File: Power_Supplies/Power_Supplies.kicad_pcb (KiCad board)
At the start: 4 copper layers, 322 parts, among them IC1 PCM1865DBT, IC2 LT8338, IC5 PCM1865DBT, J1 Line Out (Left), J10 XLR3_AudioJack3_Combo, J2 Headphone Out, J20 ACJM-MV-2, J21 Line Out (Right), J22 2171790001, J3 XLR3_AudioJack3_Combo, J4 XLR3_AudioJack3_Combo, J5 ACJM-MV-2, J6 ACJM-MV-2, J7 ACJM-MV-2, J8 FTSH-110-01-F-DV-K, J9 XLR3_AudioJack3_Combo, SW1 SW_Push, SW2 SW_Push, SW3 SW_Push, SW4 SW_Push, U1 TPS62822DLC, U10 OPA2134, U11 TPA6110A2DGN, U12 XU316-1024-TQ128-I24, U13 Si5351A-B-GT, U14 W25Q64JVSSIQ (FLASH MEMORY), U15 OPA2134, U16 SSM2019BRNZ, U17 SSM2019BRNZ, U18 OPA2134, U19 SSM2019BRNZ, U2 TPS73601DBV, U20 SSM2019BRNZ, U3 TPS62822DLC, U34 NE5532AD, U35 NE5532AD, U37 PEC11R-4030F-N0024, U4 TPS73601DBV, U5 NCP1117-5.0_SOT223, U6 TPS82140, U7 TPS62822DLC, U8 LM27761, U9 PCM1780, X1 FA-238 24.0000MB-C0 (CRYSTAL), X2 FA-238 24.0000MB-C0

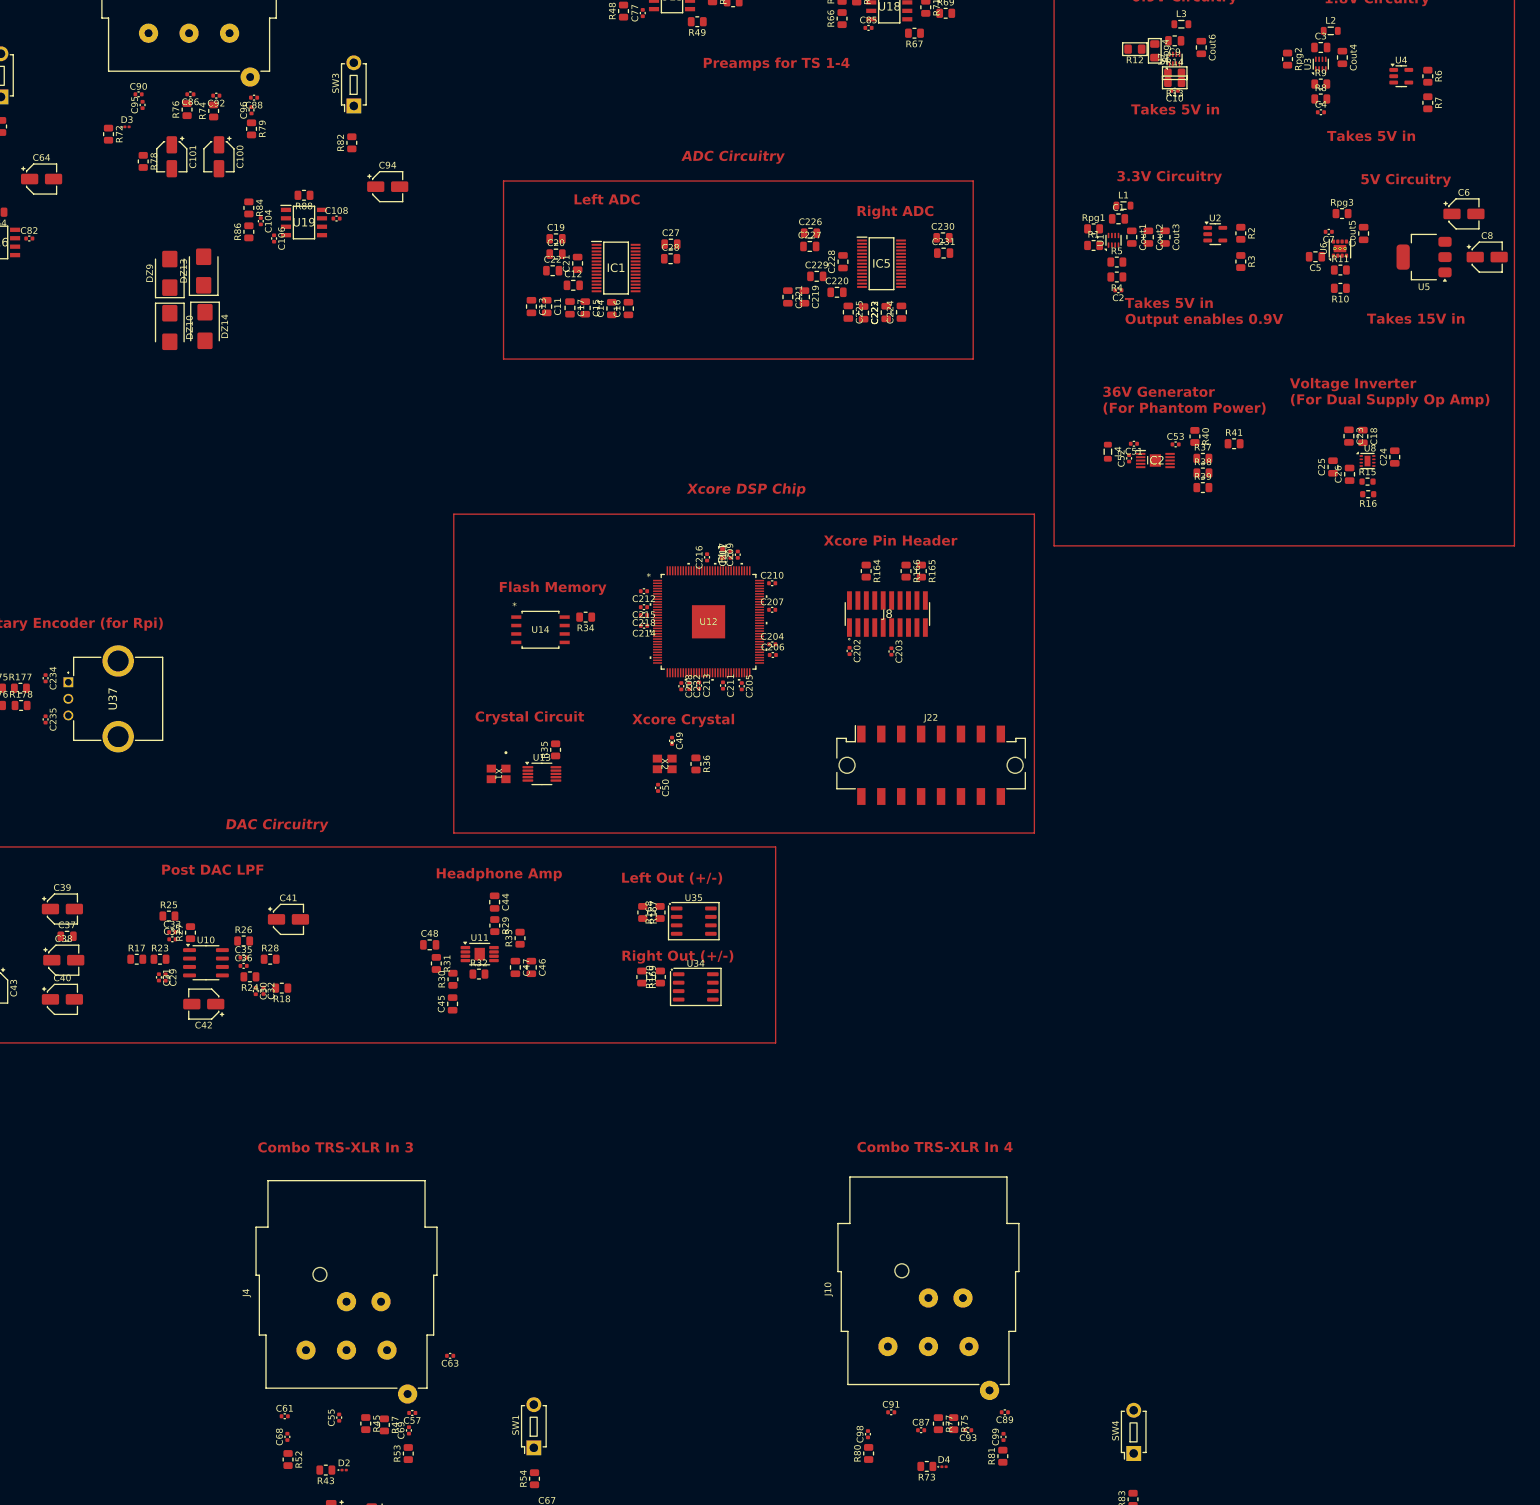
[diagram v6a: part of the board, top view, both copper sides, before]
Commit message: Added stuff for the power supply circuitry
changed all grounds to GND (same ground plane)
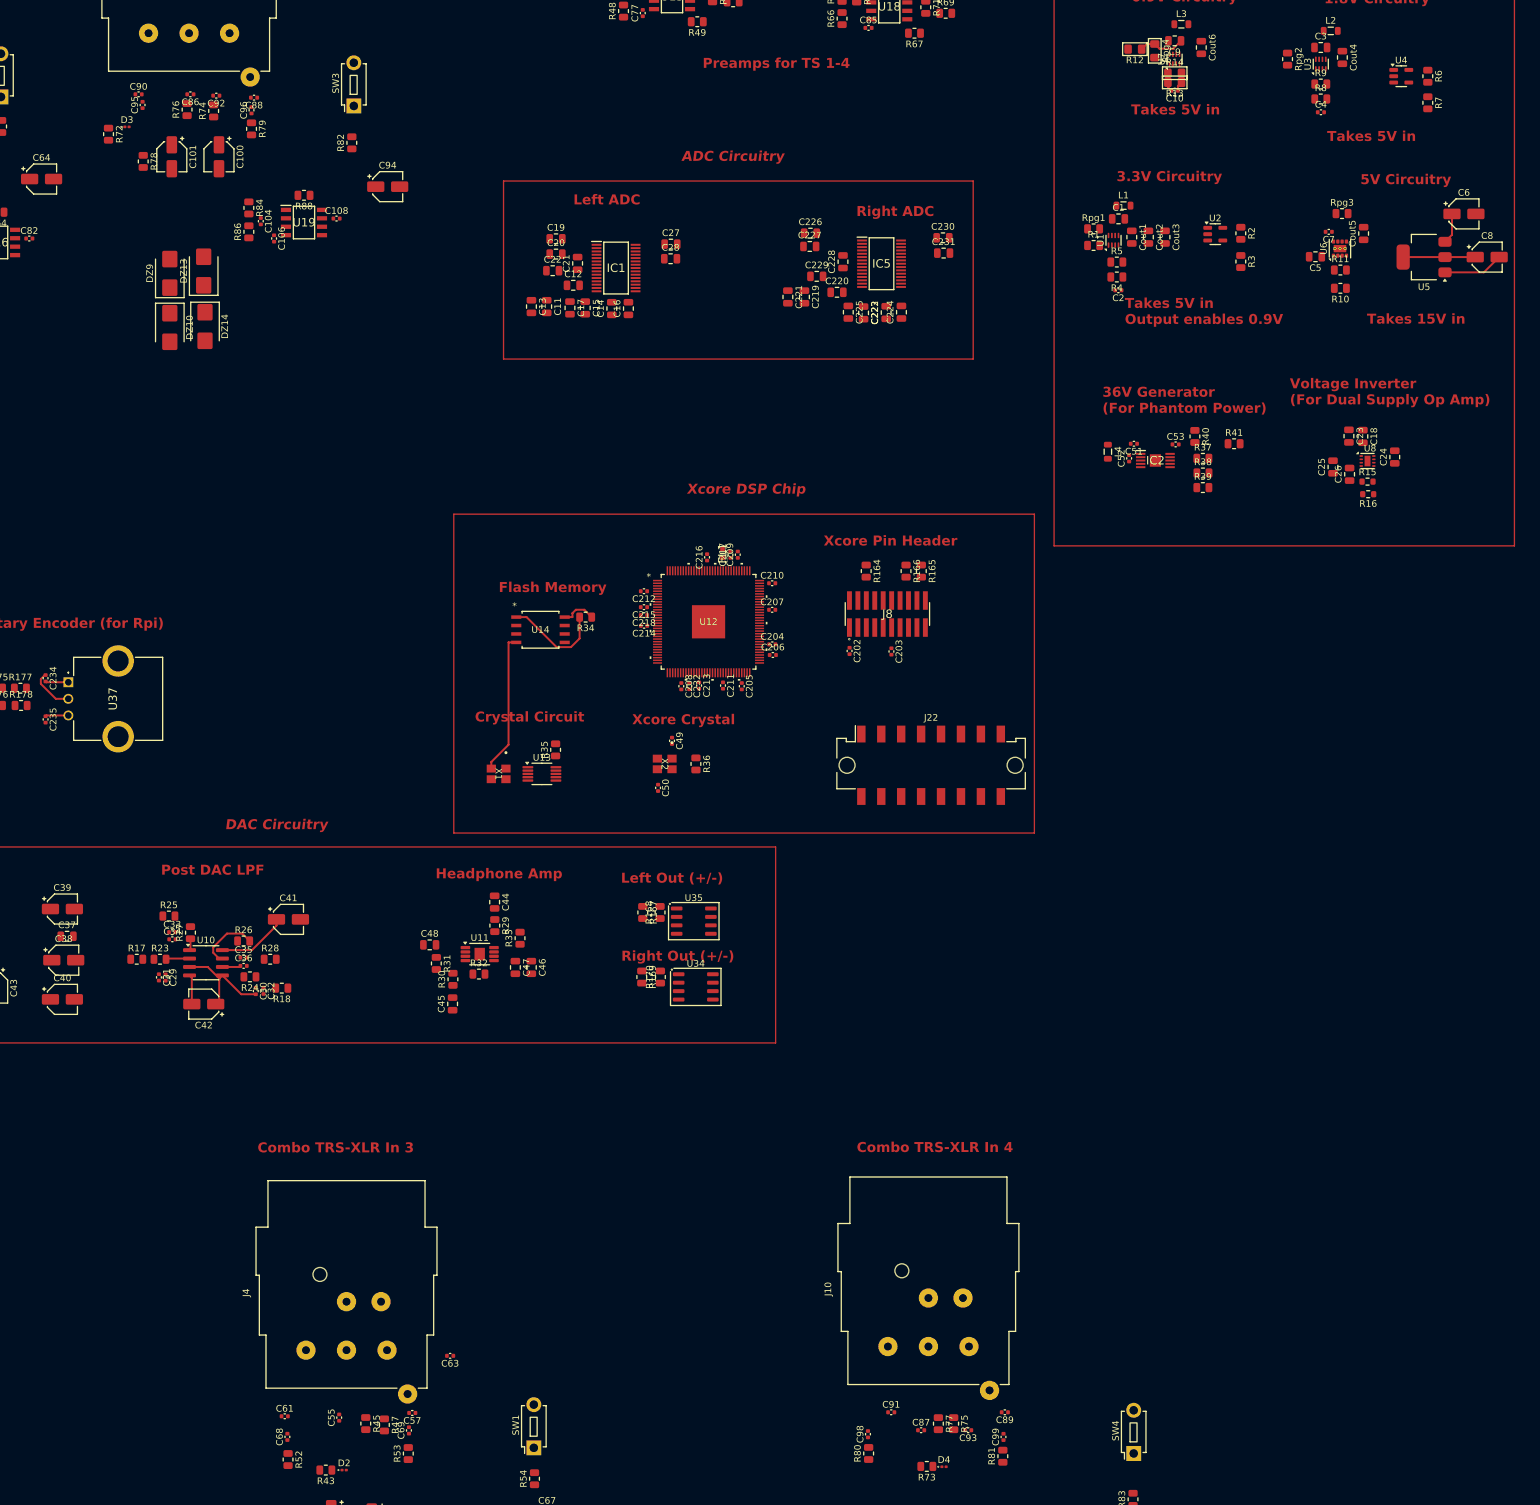
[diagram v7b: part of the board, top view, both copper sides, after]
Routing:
- net AGND: track 0.00 -> 54.7 mm
- net 5V: track 0.00 -> 17.6 mm
- net QSPI_CS_N: track 0.00 -> 15.2 mm
- net 5V_LDO: track 0.00 -> 10.8 mm
- net Net-(C35-Pad2): track 0.00 -> 9.36 mm
- net 3.3V: track 0.00 -> 5.33 mm
- net 15V: track 0.00 -> 4.63 mm
- net -5V: track 0.00 -> 4.46 mm
- net Net-(U10A--): track 0.00 -> 3.57 mm
- net Net-(U37-CHANNEL_2): track 0.00 -> 3.47 mm
- net Net-(U37-CHANNEL_1): track 0.00 -> 3.47 mm
- net /0.9V Power Supply/V_FB: track 0.00 -> 2.86 mm
- net Net-(U10B--): track 0.00 -> 2.78 mm
- net Net-(C33-Pad2): track 0.00 -> 1.77 mm
- net 0.9V: track 0.00 -> 1.48 mm

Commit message: Add files via upload
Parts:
- removed C1, C25, C3, C9: 4.7uF, Capacitor_SMD:C_0805_2012Metric
- removed C10, C2, C4: 120pF, Capacitor_SMD:C_0402_1005Metric
- removed C18: 10uF, Capacitor_SMD:C_0805_2012Metric
- removed C23, C24: 1uF, Capacitor_SMD:C_0805_2012Metric
- removed C26: 2.2uF, Capacitor_SMD:C_0805_2012Metric
- removed C5, Cout1, Cout2, Cout3, Cout4, Cout6: 22uF, Capacitor_SMD:C_0805_2012Metric
- removed C51, C52, C53: 2.2uF, Capacitor_SMD:C_0402_1005Metric
- removed C6, C8: 10uF, Capacitor_SMD:CP_Elec_4x5.8
- removed C7: 430pF, Capacitor_SMD:C_0402_1005Metric
- removed Cout5: 47uF, Capacitor_SMD:C_0805_2012Metric
- removed D1, D2, D3, D4: LED, LED_SMD:LED_0201_0603Metric
- removed IC2: LT8338, SamacSys_Parts:SOP50P490X110-11N
- removed L1, L2, L3: 470nH, Inductor_SMD:L_0805_2012Metric
- removed L4: 10uH, Inductor_SMD:L_0805_2012Metric
- removed R1: 20k, Resistor_SMD:R_0805_2012Metric
- removed R10: 523k, Resistor_SMD:R_0805_2012Metric
- removed R11, R5, R9, Rpg1, Rpg2, Rpg3: 100k, Resistor_SMD:R_0805_2012Metric
- removed R12: 10k, PCM_Resistor_SMD_AKL:R_0805_2012Metric_Pad1.15x1.40mm_HandSolder
- removed R13: 49.9k, PCM_Resistor_SMD_AKL:R_0805_2012Metric_Pad1.15x1.40mm_HandSolder
- removed R14, Rpg4: 100k, PCM_Resistor_SMD_AKL:R_0805_2012Metric_Pad1.15x1.40mm_HandSolder
- removed R15: 249k, Resistor_SMD:R_0603_1608Metric
- removed R16: 499k, Resistor_SMD:R_0603_1608Metric
- removed R2: 52.3k, Resistor_SMD:R_0805_2012Metric
- removed R3: 30.1k, Resistor_SMD:R_0805_2012Metric
- removed R37, R41: 1M, Resistor_SMD:R_0805_2012Metric
- removed R38: 162k, Resistor_SMD:R_0805_2012Metric
- removed R39: 40.2k, Resistor_SMD:R_0805_2012Metric
- removed R4: 453k, Resistor_SMD:R_0805_2012Metric
- removed R40: 301k, Resistor_SMD:R_0805_2012Metric
- removed R43: 2.2k, Resistor_SMD:R_0805_2012Metric
- removed R6: 28k, Resistor_SMD:R_0805_2012Metric
- removed R7: 56.2k, Resistor_SMD:R_0805_2012Metric
- removed R8: 200k, Resistor_SMD:R_0805_2012Metric
- removed SW1, SW2, SW3, SW4: SW_Push, Button_Switch_THT:SW_PUSH_1P1T_6x3.5mm_H5.0_APEM_MJTP1250
- removed U1, U3, U7: TPS62822DLC, Package_SON:Texas_VSON-HR-8_1.5x2mm_P0.5mm
- removed U2, U4: TPS73601DBV, Package_TO_SOT_SMD:SOT-23-5
- removed U5: NCP1117-5.0_SOT223, Package_TO_SOT_SMD:SOT-223-3_TabPin2
- removed U6: TPS82140, Package_LGA:Texas_SIL0008D_MicroSiP-8-1EP_2.8x3mm_P0.65mm_EP1.1x1.9mm_ThermalVias
- removed U8: LM27761, Package_SON:WSON-8-1EP_2x2mm_P0.5mm_EP0.9x1.6mm
- added H1: MountingHole_M3, MountingHole:MountingHole_3.2mm_M3, F.Cu at (30.8, 51.0)
- added H2: MountingHole_M3, MountingHole:MountingHole_3.2mm_M3, F.Cu at (268.5, 51.0)
- added H3: MountingHole_M3, MountingHole:MountingHole_3.2mm_M3, F.Cu at (31.0, 222.2)
- added H4: MountingHole_M3, MountingHole:MountingHole_3.2mm_M3, F.Cu at (268.5, 222.5)
- added J28: PINHD_1x2_Female, Connector_PinSocket_2.54mm:PinSocket_1x02_P2.54mm_Vertical, F.Cu at (258.4, 187.7)
- added J29: PINHD_1x2_Female, Connector_PinSocket_2.54mm:PinSocket_1x02_P2.54mm_Vertical, F.Cu at (108.6, 98.6)
- added J30: PINHD_1x2_Female, Connector_PinSocket_2.54mm:PinSocket_1x02_P2.54mm_Vertical, F.Cu at (28.1, 98.1)
- added J31: PINHD_1x2_Female, Connector_PinSocket_2.54mm:PinSocket_1x02_P2.54mm_Vertical, F.Cu at (65.2, 97.5)
- added J32: PINHD_1x2_Female, Connector_PinSocket_2.54mm:PinSocket_1x02_P2.54mm_Vertical, F.Cu at (143.7, 98.7)
- added J33: PINHD_1x3_Female, Connector_PinSocket_2.54mm:PinSocket_1x03_P2.54mm_Vertical, F.Cu at (154.7, 197.3)
- added J34: PINHD_1x1_Female, Connector_PinSocket_2.54mm:PinSocket_1x01_P2.54mm_Vertical, F.Cu at (268.4, 110.7)
- added J36: PINHD_1x2_Female, Connector_PinSocket_2.54mm:PinSocket_1x02_P2.54mm_Vertical, F.Cu at (145.3, 197.7)
- added J37: PINHD_1x3_Female, Connector_PinSocket_2.54mm:PinSocket_1x03_P2.54mm_Vertical, F.Cu at (226.3, 153.0)
- added J38: PINHD_1x1_Female, Connector_PinSocket_2.54mm:PinSocket_1x01_P2.54mm_Vertical, F.Cu at (75.8, 198.7)
- added J39: PINHD_1x1_Female, Connector_PinSocket_2.54mm:PinSocket_1x01_P2.54mm_Vertical, F.Cu at (68.7, 208.6)
- added J40: PINHD_1x1_Female, Connector_PinSocket_2.54mm:PinSocket_1x01_P2.54mm_Vertical, F.Cu at (130.6, 174.4)
- added R174: 5k1, Resistor_SMD:R_0402_1005Metric, F.Cu at (269.7, 140.5)
- added R179: 5k1, Resistor_SMD:R_0402_1005Metric, F.Cu at (269.6, 152.6)
- C13, C16, C17, C221, C224, C225: footprint Capacitor_SMD:C_0805_2012Metric -> Capacitor_SMD:C_0603_1608Metric_Pad1.08x0.95mm_HandSolder
- J10, J3, J4, J9: footprint Connector_Audio:Jack_XLR-6.35mm_Neutrik_NCJ5FI-H-0_Horizontal -> Connector_Audio:Jack_XLR-6.35mm_Neutrik_NCJ6FA-H_Horizontal
- J22: value 2171790001 -> USB_C_Receptacle_USB2.0; footprint Connector_Molex:Molex_Micro-Fit_3.0_43045-1615_2x08_P3.00mm_Vertical -> Connector_USB:USB_C_Receptacle_HRO_TYPE-C-31-M-12
- J8: footprint SamacSys_Parts:FTSH-110-XX-YYY-DV-K-A -> SamacSys_Parts:FTSH-110-XX-YYY-DV-K
- R42: value 2.2k -> 5k; footprint Resistor_SMD:R_0805_2012Metric -> Resistor_SMD:R_0402_1005Metric_Pad0.72x0.64mm_HandSolder
- R72, R73: value 2.2k -> 4.7K
- moved J2 286.3 mm to (35.0, 169.0), turned to 90 degrees
- moved J21 276.6 mm to (35.0, 193.1), turned to 90 degrees
- moved J1 275.7 mm to (35.0, 207.0), turned to 90 degrees
- moved R42 211.4 mm to (238.0, 111.8), turned to 0 degrees
- moved R175 209.5 mm to (258.5, 178.7), turned to -90 degrees
- moved R177 206.8 mm to (258.4, 183.0), turned to -90 degrees
- moved R176 206.5 mm to (255.9, 178.7), turned to -90 degrees
- moved C234 206.4 mm to (259.6, 191.3), turned to 180 degrees
- moved R178 203.7 mm to (255.8, 183.1), turned to -90 degrees
- moved U37 203.2 mm to (259.1, 194.7), turned to 180 degrees
- moved C235 198.9 mm to (253.4, 191.3), turned to 180 degrees
- moved C97 187.4 mm to (148.3, 102.2), turned to -90 degrees
- moved R83 184.0 mm to (149.0, 96.0), turned to 180 degrees
- moved C93 170.2 mm to (176.2, 85.2), turned to -90 degrees
- moved C105 169.3 mm to (156.4, 110.1)
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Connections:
- C106 pad 1: -5V -> -12V
- C106 pad 2: AGND -> GND
- C107 pad 1: -5V -> -12V
- C107 pad 2: AGND -> GND
- C108 pad 1: 5V -> 12V
- C108 pad 2: AGND -> GND
- C109 pad 1: 5V -> 12V
- C109 pad 2: AGND -> GND
- C11 pad 1: AGND -> GND
- C11 pad 2: AGND -> GND
- C12 pad 1: 3.3V_LDO -> 3.3V
- C13 pad 1: AGND -> GND
- C13 pad 2: AGND -> GND
- C14 pad 1: AGND -> GND
- C15 pad 2: AGND -> GND
- C16 pad 1: AGND -> GND
- C17 pad 2: AGND -> GND
- C202 pad 2: AGND -> GND
- C203 pad 2: AGND -> GND
- C204 pad 1: 1.8V_LDO -> 1.8V
- C204 pad 2: AGND -> GND
- C205 pad 1: 3.3V_LDO -> 3.3V
- C205 pad 2: AGND -> GND
- C206 pad 2: AGND -> GND
- C207 pad 2: AGND -> GND
- C208 pad 2: AGND -> GND
- C209 pad 2: AGND -> GND
- C21 pad 1: AGND -> GND
- C210 pad 2: AGND -> GND
- C211 pad 2: AGND -> GND
- C212 pad 2: AGND -> GND
- C213 pad 2: AGND -> GND
- C214 pad 2: AGND -> GND
- C215 pad 2: AGND -> GND
- C216 pad 2: AGND -> GND
- C217 pad 2: AGND -> GND
- C218 pad 2: AGND -> GND
- C219 pad 1: AGND -> GND
- C219 pad 2: AGND -> GND
- C22 pad 1: AGND -> GND
- C220 pad 1: 3.3V_LDO -> 3.3V
- C221 pad 1: AGND -> GND
- C221 pad 2: AGND -> GND
- C222 pad 1: AGND -> GND
- C223 pad 2: AGND -> GND
- C224 pad 1: AGND -> GND
- C225 pad 2: AGND -> GND
- C228 pad 1: AGND -> GND
- C229 pad 1: AGND -> GND
- C232 pad 2: AGND -> GND
- C234 pad 1: AGND -> GND
- C235 pad 2: AGND -> GND
- C29 pad 2: AGND -> GND
- C30 pad 2: AGND -> GND
- C31 pad 2: AGND -> GND
- C32 pad 2: AGND -> GND
- C37 pad 1: 5V_LDO -> 5V
- C37 pad 2: AGND -> GND
- C38 pad 1: 5V_LDO -> 5V
- C38 pad 2: AGND -> GND
- C41 pad 1: 5V -> 12V
- C41 pad 2: AGND -> GND
- C42 pad 1: AGND -> GND
- C42 pad 2: -5V -> -12V
- C43 pad 2: AGND -> GND
- C44 pad 1: LEFT_IN -> Net-(C44-Pad1)
- C44 pad 2: Net-(C44-Pad2) -> LEFT_IN
- C46 pad 2: AGND -> GND
- C47 pad 2: AGND -> GND
- C48 pad 2: AGND -> GND
- C49 pad 1: AGND -> GND
- C50 pad 2: AGND -> GND
- C54 pad 1: AGND -> GND
- C55 pad 1: AGND -> GND
- C56 pad 1: AGND -> GND
- C57 pad 1: AGND -> GND
- C60 pad 1: AGND -> GND
- C61 pad 1: AGND -> GND
- C62 pad 1: AGND -> GND
- C63 pad 1: AGND -> GND
- C64 pad 2: AGND -> GND
- C67 pad 2: AGND -> GND
- C76 pad 1: AGND -> GND
- C76 pad 2: 5V -> 12V
- C77 pad 1: AGND -> GND
- C77 pad 2: -5V -> -12V
- C78 pad 1: -5V -> -12V
- C78 pad 2: AGND -> GND
- C79 pad 1: -5V -> -12V
- C79 pad 2: AGND -> GND
- C82 pad 1: 5V -> 12V
- C82 pad 2: AGND -> GND
- C83 pad 1: 5V -> 12V
- C83 pad 2: AGND -> GND
- C84 pad 1: AGND -> GND
- C84 pad 2: 5V -> 12V
- C85 pad 1: AGND -> GND
- C85 pad 2: -5V_1 -> -12V
- C86 pad 1: AGND -> GND
- C87 pad 1: AGND -> GND
- C88 pad 1: AGND -> GND
- C89 pad 1: AGND -> GND
- C90 pad 1: AGND -> GND
- C91 pad 1: AGND -> GND
- C92 pad 1: AGND -> GND
- C93 pad 1: AGND -> GND
- C94 pad 2: AGND -> GND
- C97 pad 2: AGND -> GND
- DZ10 pad 2: AGND -> GND
- DZ12 pad 2: AGND -> GND
- DZ14 pad 2: AGND -> GND
- DZ16 pad 2: AGND -> GND
- DZ2 pad 2: AGND -> GND
- DZ4 pad 2: AGND -> GND
- DZ6 pad 2: AGND -> GND
- DZ8 pad 2: AGND -> GND
- IC1 pad 12: AGND -> GND
- IC1 pad 25: ADDRESS -> GND
- IC1 pad 26: AGND -> GND
- IC1 pad 7: AGND -> GND
- IC5 pad 12: AGND -> GND
- IC5 pad 25: ADDRESS -> Net-(IC5-MS/AD)
- IC5 pad 26: AGND -> GND
- IC5 pad 7: AGND -> GND
- J1 pad S: AGND -> GND
- J10 pad 1: AGND -> GND
- J10 pad S: AGND -> GND
- J2 pad S: AGND -> GND
- J20 pad 1: AGND -> GND
- J21 pad S: AGND -> GND
- J3 pad 1: AGND -> GND
- J3 pad S: AGND -> GND
- J4 pad 1: AGND -> GND
- J4 pad S: AGND -> GND
- J5 pad 1: AGND -> GND
- J6 pad 1: AGND -> GND
- J7 pad 1: AGND -> GND
- J8 pad 13: AGND -> GND
- J8 pad 15: AGND -> GND
- J8 pad 17: AGND -> GND
- J8 pad 19: AGND -> GND
- J8 pad 3: AGND -> GND
- J8 pad 5: AGND -> GND
- J8 pad 7: AGND -> GND
- J8 pad 9: AGND -> GND
- J9 pad 1: AGND -> GND
- J9 pad S: AGND -> GND
- R29 pad 1: Net-(C44-Pad2) -> Net-(C44-Pad1)
- R31 pad 2: AGND -> GND
- R42 pad 1: Net-(D1-Pad1) -> Net-(IC5-MS/AD)
- R42 pad 2: AGND -> 3.3V
- R48 pad 1: AGND -> GND
- R49 pad 1: AGND -> GND
- R55 pad 2: AGND -> GND
- R57 pad 2: AGND -> GND
- R58 pad 1: INST1_OUT -> AIN_6
- R59 pad 1: INST2_OUT -> AIN_5
- R60 pad 1: AGND -> GND
- R61 pad 1: AGND -> GND
- R62 pad 1: AGND -> GND
- R63 pad 1: AGND -> GND
- R66 pad 1: AGND -> GND
- R67 pad 1: AGND -> GND
- R68 pad 2: AGND -> GND
- R69 pad 2: AGND -> GND
- R70 pad 1: INST3_OUT -> AIN_8
- R71 pad 1: INST4_OUT -> AIN_7
- R72 pad 1: Net-(D3-Pad1) -> SCL
- R72 pad 2: AGND -> 3.3V
- R73 pad 1: Net-(D4-Pad1) -> SDA
- R73 pad 2: AGND -> 3.3V
- R84 pad 1: AGND -> GND
- R85 pad 1: AGND -> GND
- R86 pad 1: AGND -> GND
- R87 pad 1: AGND -> GND
- U10 pad 3: AGND -> GND
- U10 pad 4: -5V -> -12V
- U10 pad 5: AGND -> GND
- U10 pad 8: 5V -> 12V
- U11 pad 2: AGND -> GND
- U11 pad 9: AGND -> GND
- U12 pad 10: 1.8V_LDO -> 1.8V
- U12 pad 107: unconnected-(U12B-X1D24-Pad107) -> DATA_OUT_1
- U12 pad 108: unconnected-(U12B-X1D25-Pad108) -> DATA_OUT_2
- U12 pad 109: 1.8V_LDO -> 1.8V
- U12 pad 121: 1.8V_LDO -> 1.8V
- U12 pad 129: AGND -> GND
- U12 pad 16: unconnected-(U12A-X1D39-Pad16) -> DATA
- U12 pad 17: 1.8V_LDO -> 1.8V
- U12 pad 20: unconnected-(U12A-X1D01-Pad20) -> LRCK
- U12 pad 24: AGND -> GND
- U12 pad 27: AGND -> GND
- U12 pad 30: AGND -> GND
- U12 pad 35: 1.8V_LDO -> 1.8V
- U12 pad 40: AGND -> GND
- U12 pad 42: AGND -> GND
- U12 pad 43: AGND -> GND
- U12 pad 52: AGND -> GND
- U12 pad 56: 1.8V_LDO -> 1.8V
- U12 pad 61: 3.3V_LDO -> 3.3V
- U12 pad 62: 1.8V_LDO -> 1.8V
- U12 pad 7: unconnected-(U12A-X0D11-Pad7) -> MCLK
- U12 pad 72: 1.8V_LDO -> 1.8V
- U12 pad 89: 1.8V_LDO -> 1.8V
- U12 pad 93: unconnected-(U12B-X0D35-Pad93) -> SCL
- U12 pad 94: unconnected-(U12B-X0D36-Pad94) -> SDA
- U13 pad 8: AGND -> GND
- U14 pad 4: AGND -> GND
- U15 pad 1: INST1_OUT -> AIN_6
- U15 pad 4: -5V -> -12V
- U15 pad 7: INST2_OUT -> AIN_5
- U15 pad 8: 5V -> 12V
- U16 pad 4: -5V -> -12V
- U16 pad 5: AGND -> GND
- U16 pad 6: PREAMP1_OUT -> AIN_1
- U16 pad 7: 5V -> 12V
- U17 pad 4: -5V -> -12V
- U17 pad 5: AGND -> GND
- U17 pad 6: PREAMP3_OUT -> AIN_3
- U17 pad 7: 5V -> 12V
- U18 pad 1: INST3_OUT -> AIN_8
- U18 pad 4: -5V_1 -> -12V
- U18 pad 7: INST4_OUT -> AIN_7
- U18 pad 8: 5V -> 12V
- U19 pad 4: -5V -> -12V
- U19 pad 5: AGND -> GND
- U19 pad 6: PREAMP2_OUT -> AIN_2
- U19 pad 7: 5V -> 12V
- U20 pad 4: -5V -> -12V
- U20 pad 5: AGND -> GND
- U20 pad 6: PREAMP4_OUT -> AIN_4
- U20 pad 7: 5V -> 12V
- U34 pad 3: AGND -> GND
- U34 pad 4: -5V -> -12V
- U34 pad 8: 5V -> 12V
- U35 pad 3: AGND -> GND
- U35 pad 4: -5V -> -12V
- U35 pad 8: 5V -> 12V
- U37 pad C1: AGND -> GND
- U9 pad 1: ZERO_L -> Net-(U9-ZEROL)
- U9 pad 11: 5V_LDO -> 5V
- U9 pad 12: AGND -> GND
- U9 pad 16: ZERO_R -> Net-(U9-ZEROR)
- U9 pad 2: MODE_CONTROL_SELECT -> Net-(U9-~{MS})
- U9 pad 3: MODE_CONTROL_CLOCK -> Net-(U9-MC)
- U9 pad 4: MODE_CONTROL_DATA -> Net-(U9-MD)
- X1 pad 2: AGND -> GND
- X1 pad 4: AGND -> GND
- X2 pad 2: AGND -> GND
- X2 pad 4: AGND -> GND
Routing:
- net -12V: track 0.00 -> 506.3 mm, vias 0 -> 11
- net 12V: track 0.00 -> 402.5 mm, vias 0 -> 9
- net 3.3V: track 5.33 -> 403.1 mm, vias 0 -> 9
- net GND: track 0.00 -> 373.1 mm, vias 0 -> 241
- net 5V: track 17.6 -> 267.2 mm, vias 0 -> 3
- net SCL: track 0.00 -> 192.8 mm, vias 0 -> 6
- net BCK: track 0.00 -> 173.3 mm, vias 0 -> 3
- net SDA: track 0.00 -> 172.6 mm, vias 0 -> 2
- net LRCK: track 0.00 -> 165.8 mm, vias 0 -> 6
- net 0.9V: track 1.48 -> 134.5 mm, vias 0 -> 6
- net 1.8V: track 0.00 -> 126.2 mm, vias 0 -> 4
- net MCLK: track 0.00 -> 118.4 mm
- net DATA: track 0.00 -> 104.2 mm, vias 0 -> 2
- net USB_DN: track 0.00 -> 88.4 mm, vias 0 -> 2
- net LEFT_IN: track 0.00 -> 87.8 mm, vias 0 -> 2
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- added copper zone on F.Cu, net GND
- added copper zone on In1.Cu, net GND
- added copper zone on In2.Cu, net GND
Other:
- board outline added: 247.8 x 181.5 mm
- board text added: "-12V"
- board text added: "0.9V"
- board text added: "1.8V"
- board text added: "12V"
- board text added: "3.3V"
- board text added: "36V"
- board text added: "40mm Apart"
- board text added: "5V"
- board text added: "GND"
- board text added: "Headphone Amplifier"
- board text added: "L"
- board text added: "Line Out"
- board text added: "Post-DAC LPF"
- board text added: "R"
- board text added: "Rotary Encoder"
- board text added: "USB"
- board text added: "Xcore Chip"
- board text removed: "0.9V Circuitry"
- board text removed: "1.8V Circuitry"
- board text removed: "3.3V Circuitry"
- board text removed: "36V Generator (For Phantom Power)"
- board text removed: "5V Circuitry"
- board text removed: "ADC Circuitry"
- board text removed: "Combo TRS-XLR In 1"
- board text removed: "Combo TRS-XLR In 2"
- board text removed: "Combo TRS-XLR In 3"
- board text removed: "Combo TRS-XLR In 4"
- board text removed: "Crystal Circuit"
- board text removed: "DAC Circuitry"
- board text removed: "Headphone Amp"
- board text removed: "Line Out L R"
- board text removed: "Post DAC LPF"
- board text removed: "Power Input Circuitry"
- board text removed: "Preamps for TS 1-4"
- board text removed: "Rotary Encoder (for Rpi)"
- board text removed: "TS in 1/2"
- board text removed: "TS in 3/4"
- board text removed: "Takes 15V in"
- board text removed: "Takes 5V in"
- board text removed: "Takes 5V in Output enables 0.9V"
- board text removed: "Voltage Inverter (For Dual Supply Op Amp)"
- board text removed: "Xcore Crystal"
- board text removed: "Xcore DSP Chip"
